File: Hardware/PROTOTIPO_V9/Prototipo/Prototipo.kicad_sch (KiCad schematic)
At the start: 2 parts, among them U1 YAAJ_BluePill_Part_Like_SWD_B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, U3 YAAJ_BlackPill_Part_Like_SWD_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

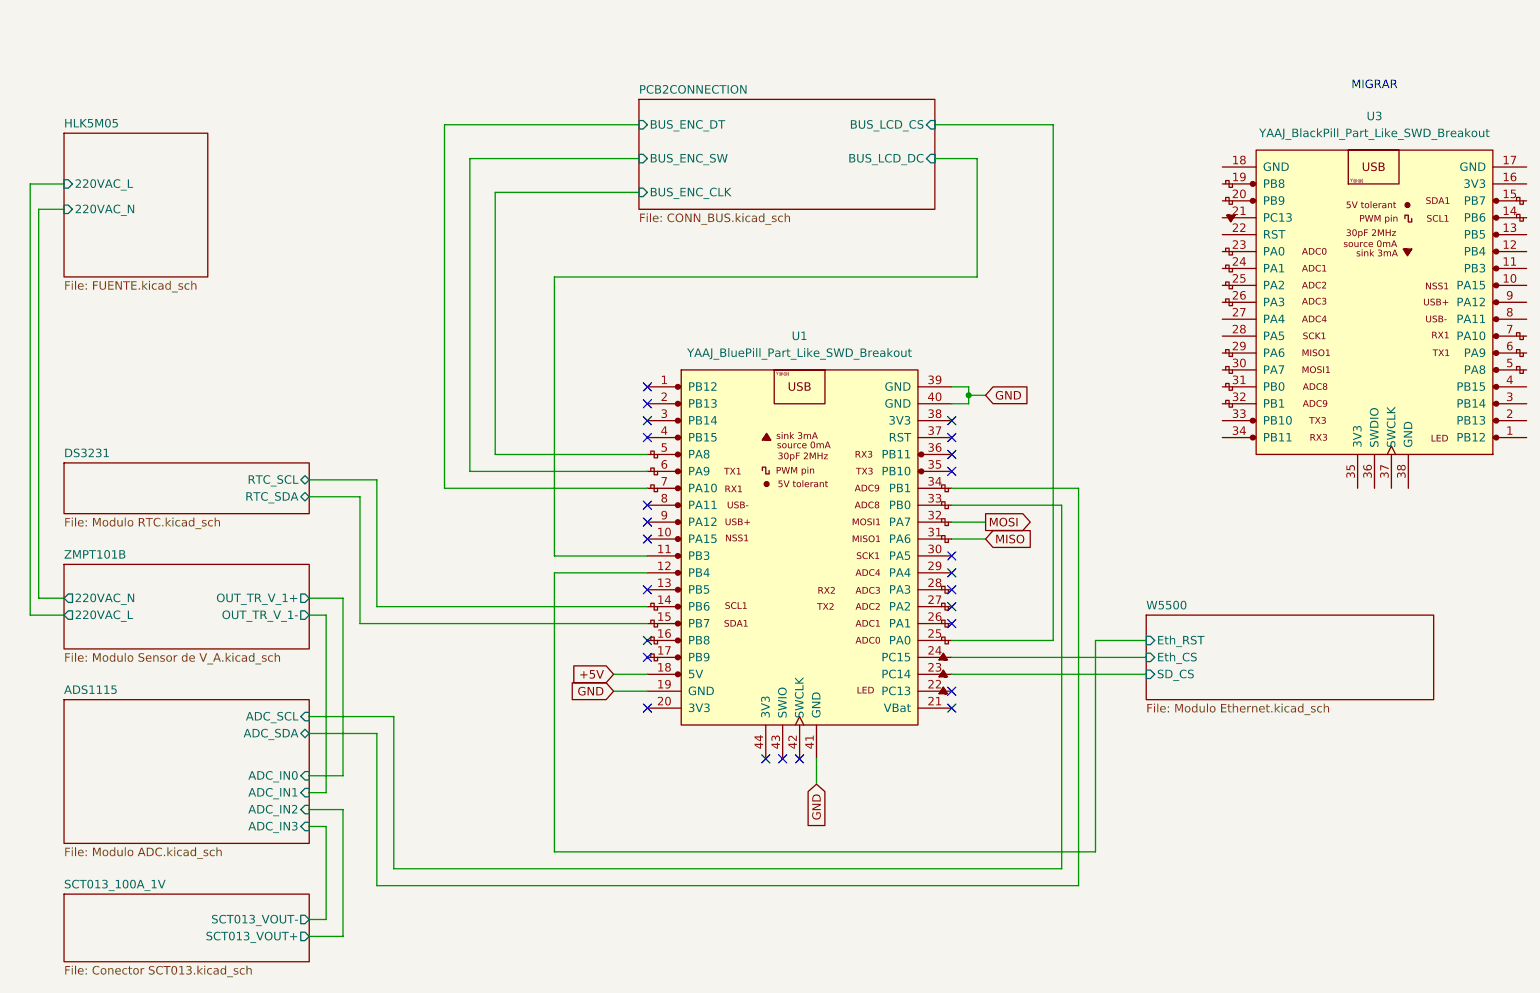
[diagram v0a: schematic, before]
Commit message: Migración de sch a BlackPill
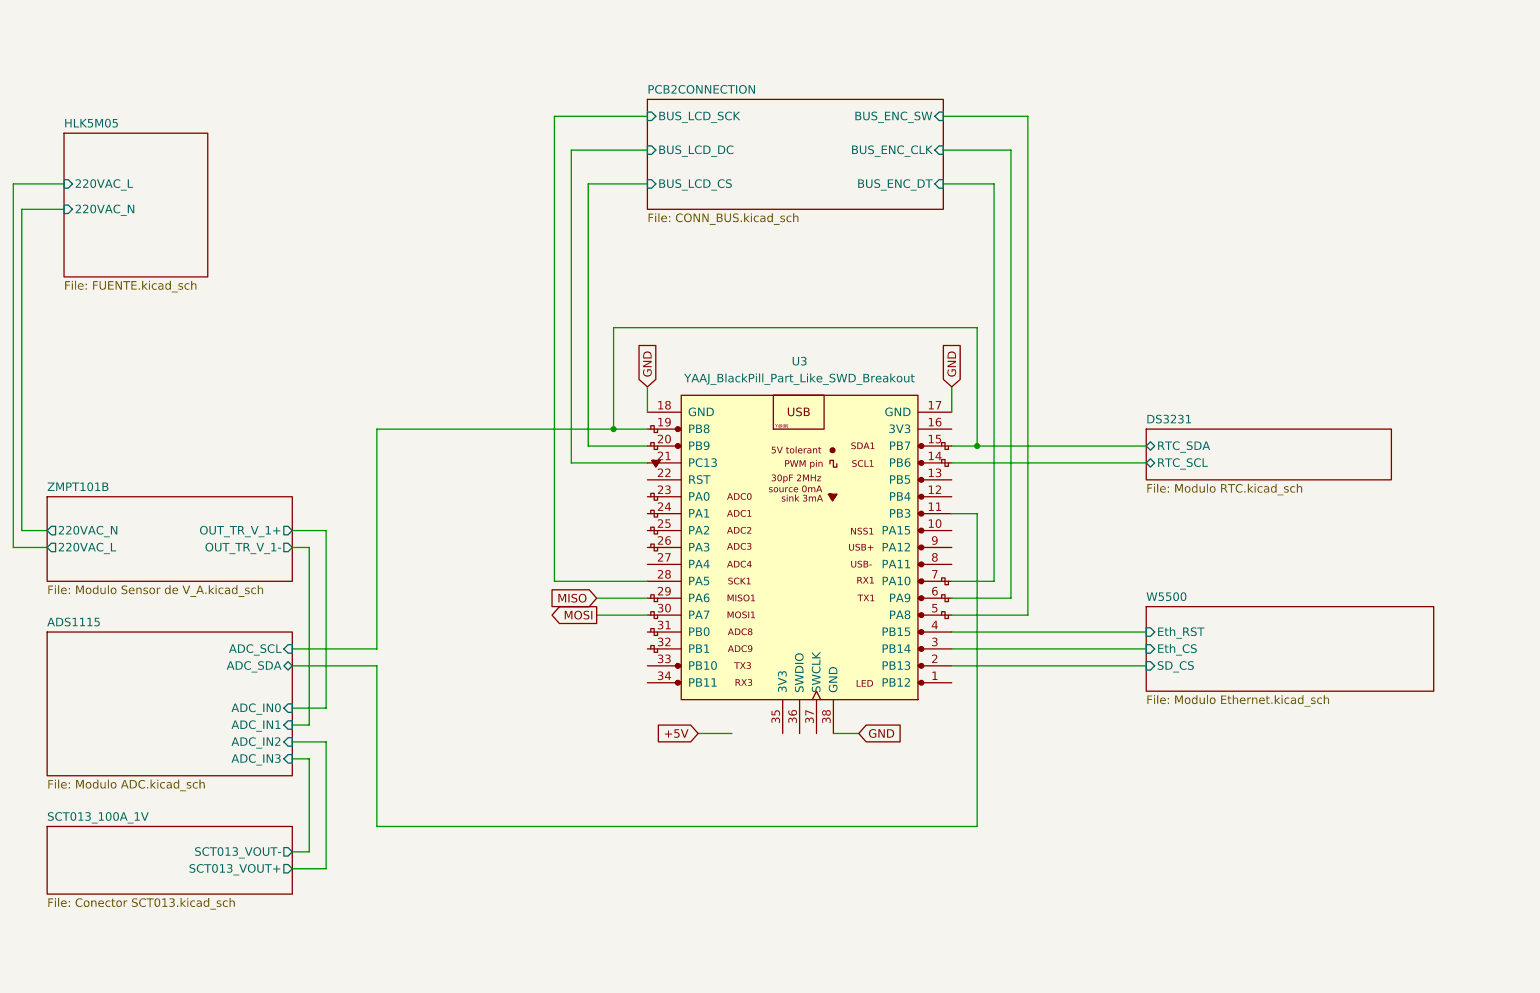
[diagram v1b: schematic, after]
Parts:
- removed U1: YAAJ_BluePill_Part_Like_SWD_Breakout, footprints_proyecto:YAAJ_BluePill_1, symbol YAAJ_BluePill_Part_Like_SWD_Breakout:YAAJ_BluePill_Part_Like_SWD_Breakout
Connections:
- net ADS1115/ADC_SCL: now also U3.15 (PB7), U3.19 (PB8)
- net ADS1115/ADC_SDA: now also U3.11 (PB3)
- net DS3231/RTC_SCL: now also U3.14 (PB6)
- net GND: now also U3.17 (GND), U3.18 (GND), U3.38 (GND)
- net MISO: now also U3.29 (PA6)
- net MOSI: now also U3.30 (PA7)
- net PCB2CONNECTION/BUS_ENC_CLK: now also U3.6 (PA9)
- net PCB2CONNECTION/BUS_ENC_DT: now also U3.7 (PA10)
- net PCB2CONNECTION/BUS_ENC_SW: now also U3.5 (PA8)
- net PCB2CONNECTION/BUS_LCD_CS: now also U3.20 (PB9)
- net PCB2CONNECTION/BUS_LCD_DC: now also U3.21 (PC13)
- net W5500/Eth_CS: now also U3.3 (PB14)
- net W5500/Eth_RST: now also U3.4 (PB15)
- net W5500/SD_CS: now also U3.2 (PB13)
- net PCB2CONNECTION/BUS_LCD_SCK: now reaches U3.28 (PA5)
- no-connect marks 25 -> 0
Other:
- sheet PCB2CONNECTION ports: added BUS_LCD_SCK; removed none
- note removed: "MIGRAR"
- moved on the sheet: U3

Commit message: Shc final y ruteo de PCB
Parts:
- added JP1, JP2, JP3, JP4: Jumper_2_Bridged, Connector_PinHeader_2.54mm:PinHeader_1x02_P2.54mm_Vertical, symbol Jumper:Jumper_2_Bridged
- added R5, R6: 1K5, Resistor_THT:R_Axial_DIN0207_L6.3mm_D2.5mm_P10.16mm_Horizontal, symbol Device:R_Small_US
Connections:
- net +5V: now also U3.20 (5V), U3.38 (5V)
- net ADS1115/ADC_IN0: now also JP1.1 (A)
- net ADS1115/ADC_IN1: now also JP2.1 (A)
- net ADS1115/ADC_SCL: now also JP3.1 (A); no longer U3.15 (PB7), U3.19 (PB8)
- net ADS1115/ADC_SDA: now also JP4.1 (A); no longer U3.11 (PB3)
- net DS3231/RTC_SCL: now also U3.36 (PB8), JP3.2 (B), R6.2; no longer U3.14 (PB6)
- net GND: now also U3.19 (GND), U3.39 (GND); no longer U3.17 (GND), U3.18 (GND), U3.38 (GND)
- net MISO: now also U3.23 (PB14); no longer U3.29 (PA6)
- net MOSI: now also U3.24 (PB15); no longer U3.30 (PA7)
- net PCB2CONNECTION/BUS_ENC_CLK: now also U3.34 (PB6); no longer U3.6 (PA9)
- net PCB2CONNECTION/BUS_ENC_DT: now also U3.35 (PB7); no longer U3.7 (PA10)
- net PCB2CONNECTION/BUS_ENC_SW: now also U3.4 (PC15); no longer U3.5 (PA8)
- net PCB2CONNECTION/BUS_LCD_CS: now also U3.21 (PB12); no longer U3.20 (PB9)
- net PCB2CONNECTION/BUS_LCD_DC: now also U3.25 (PA8); no longer U3.21 (PC13)
- net W5500/Eth_CS: now also U3.33 (PB5); no longer U3.3 (PB14)
- net W5500/Eth_RST: now also U3.3 (PC14); no longer U3.4 (PB15)
- net W5500/SD_CS: now also U3.31 (PB3); no longer U3.2 (PB13)
- net SCK: now reaches U3.22 (PB13)
- net DS3231/RTC_SDA: now reaches U3.37 (PB9)
- net DS3231/RTC_SDA: now also JP4.2 (B), R5.2
- net PCB2CONNECTION/BUS_LCD_SCK: no longer names the net of U3.28 (PA11)
- new net: JP1.2 (B), U3.6 (PA0)
- new net: JP2.2 (B), U3.7 (PA1)
- new net +3V3: R5.1, R6.1
- new net PCB2CONNECTION/BUS_LCD_RST: U3.17 (PB10)
- no-connect marks 0 -> 24
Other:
- sheet ADS1115 ports: added none; removed ADC_IN2, ADC_IN3
- sheet PCB2CONNECTION ports: added BUS_LCD_RST; removed BUS_LCD_SCK
- sheet SCT013_100A_1V ports: added SCT013_VOUT; removed SCT013_VOUT+, SCT013_VOUT-
- sheet ZMPT101B ports: added OUT_TR_V_1; removed OUT_TR_V_1+, OUT_TR_V_1-
